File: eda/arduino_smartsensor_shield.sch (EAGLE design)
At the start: 10 parts, among them J1 ARDUINO_R3_SHIELD, J2 ISP

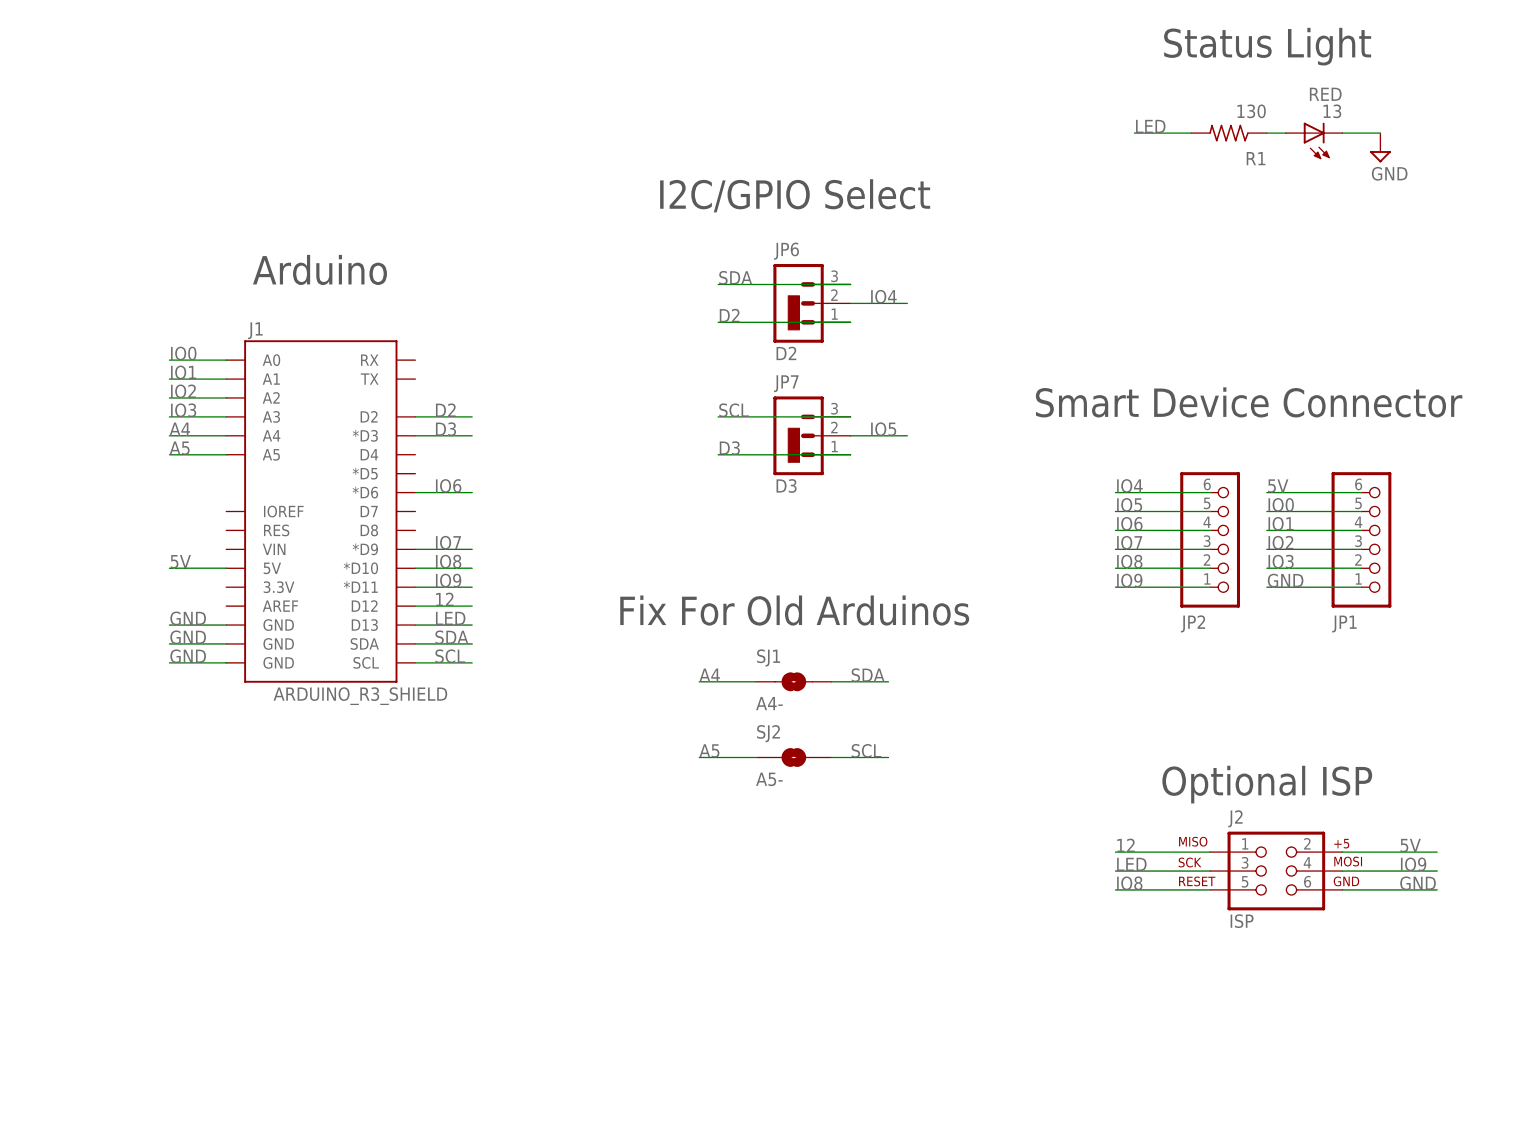
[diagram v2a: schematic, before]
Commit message: Revision B of Arduino smart device shield
- Add a connector for an external AVR programmer
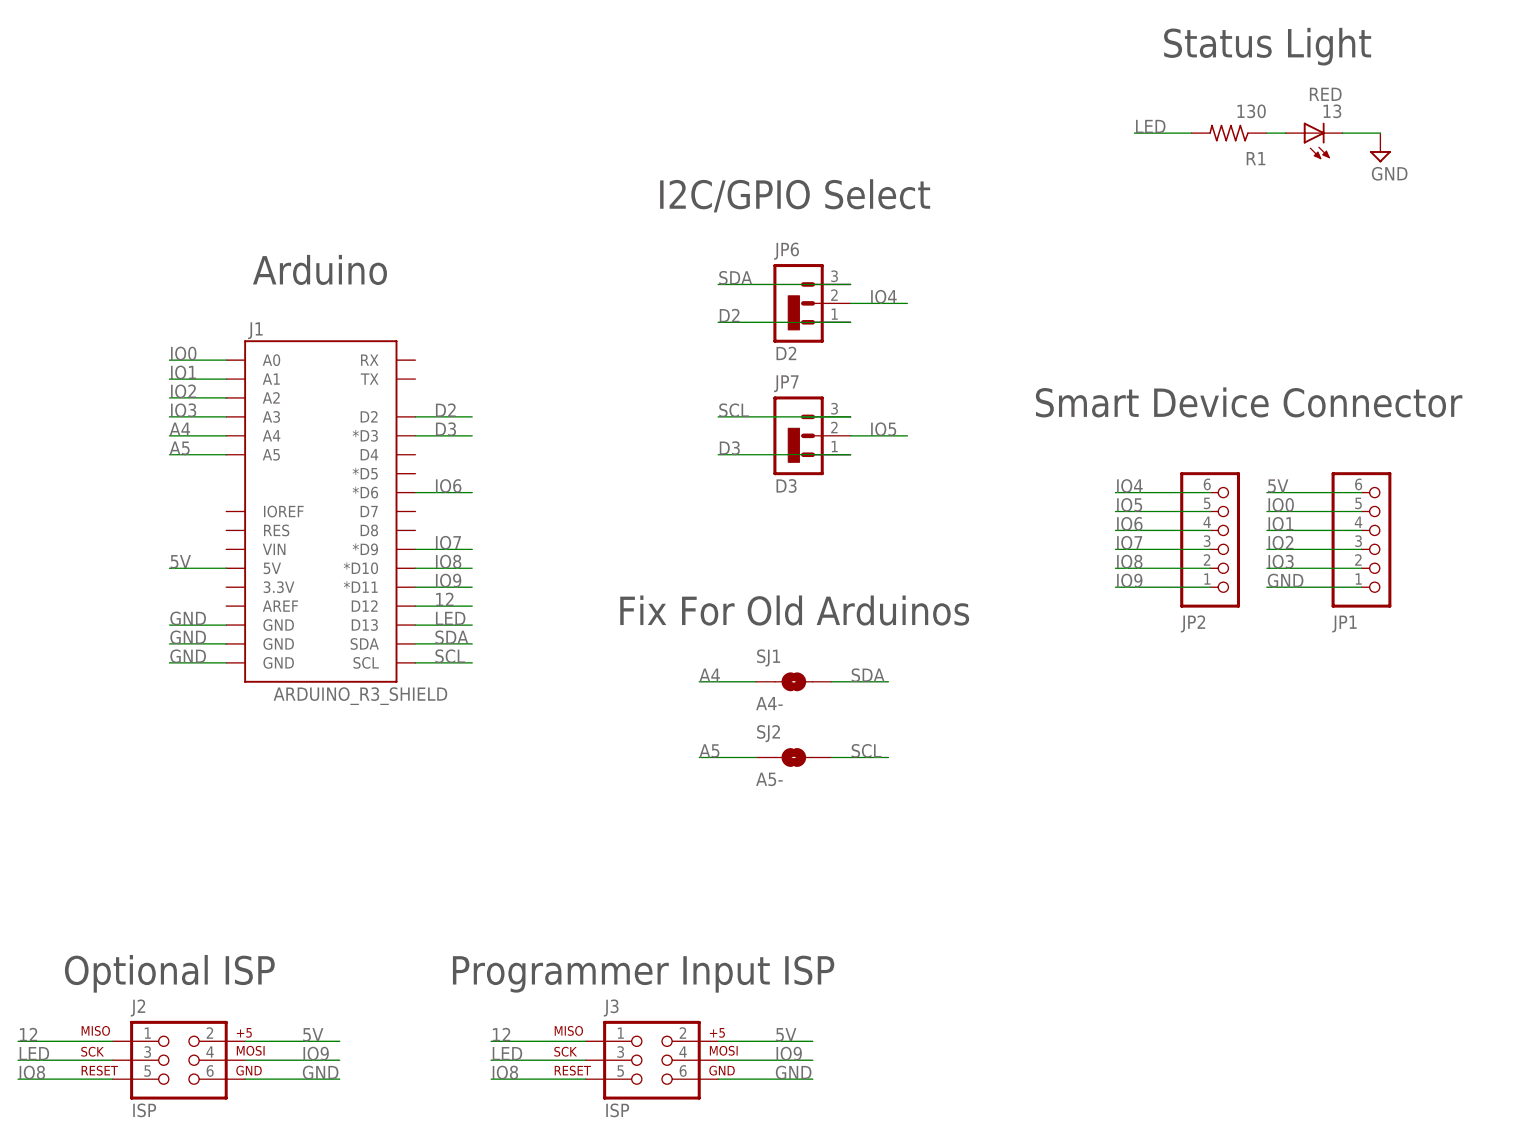
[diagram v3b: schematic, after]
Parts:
- added J3: ISP, pie:AVR_SPI_PRG_6PTH
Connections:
- net 12: now also J3.1
- net 5V: now also J3.2
- net GND: now also J3.6
- net IO8: now also J3.5
- net IO9: now also J3.4
- net LED: now also J3.3
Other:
- note added: "Programmer Input ISP"
- moved on the sheet: J2
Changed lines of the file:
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@@
 <part name="FRAME1" library="pie" deviceset="FRAME-LETTER" device="">
 <attribute name="AUTHOR" value="Casey Duckering"/>
-<attribute name="REVISION" value="1A"/>
+<attribute name="REVISION" value="1B"/>
 </part>
 <part name="R1" library="pie" deviceset="R-US_" device="R0603" value="130"/>
@@
 <part name="JP2" library="pie" deviceset="PINHD-1X6" device=""/>
 <part name="J2" library="pie" deviceset="AVR_SPI_PRG_6" device="PTH" value="ISP"/>
+<part name="J3" library="pie" deviceset="AVR_SPI_PRG_6" device="PTH" value="ISP"/>
 </parts>
 <sheets>
@@
 <text x="180.34" y="109.22" size="3.81" layer="97" font="vector" ratio="15" align="bottom-center">Smart Device Connector</text>
 <text x="182.88" y="157.48" size="3.81" layer="97" font="vector" ratio="15" align="bottom-center">Status Light</text>
-<text x="182.88" y="58.42" size="3.81" layer="97" font="vector" ratio="15" align="bottom-center">Optional ISP</text>
+<text x="35.56" y="33.02" size="3.81" layer="97" font="vector" ratio="15" align="bottom-center">Optional ISP</text>
+<text x="99.06" y="33.02" size="3.81" layer="97" font="vector" ratio="15" align="bottom-center">Programmer Input ISP</text>
 </plain>
 <instances>
@@
 <instance part="JP1" gate="A" x="195.58" y="92.71" rot="MR180"/>
 <instance part="JP2" gate="A" x="175.26" y="92.71" rot="MR180"/>
-<instance part="J2" gate="G$1" x="182.88" y="48.26"/>
+<instance part="J2" gate="G$1" x="35.56" y="22.86"/>
+<instance part="J3" gate="G$1" x="99.06" y="22.86"/>
 </instances>
 <busses>
@@
 <segment>
 <pinref part="J2" gate="G$1" pin="6"/>
-<wire x1="205.74" y1="45.72" x2="193.04" y2="45.72" width="0.1524" layer="91"/>
-<label x="200.66" y="45.72" size="1.778" layer="95"/>
+<wire x1="58.42" y1="20.32" x2="45.72" y2="20.32" width="0.1524" layer="91"/>
+<label x="53.34" y="20.32" size="1.778" layer="95"/>
+</segment>
+<segment>
+<pinref part="J3" gate="G$1" pin="6"/>
+<wire x1="121.92" y1="20.32" x2="109.22" y2="20.32" width="0.1524" layer="91"/>
+<label x="116.84" y="20.32" size="1.778" layer="95"/>
 </segment>
 </net>
@@
 <segment>
 <pinref part="J2" gate="G$1" pin="2"/>
-<wire x1="205.74" y1="50.8" x2="193.04" y2="50.8" width="0.1524" layer="91"/>
-<label x="200.66" y="50.8" size="1.778" layer="95"/>
+<wire x1="58.42" y1="25.4" x2="45.72" y2="25.4" width="0.1524" layer="91"/>
+<label x="53.34" y="25.4" size="1.778" layer="95"/>
+</segment>
+<segment>
+<pinref part="J3" gate="G$1" pin="2"/>
+<wire x1="121.92" y1="25.4" x2="109.22" y2="25.4" width="0.1524" layer="91"/>
+<label x="116.84" y="25.4" size="1.778" layer="95"/>
 </segment>
 </net>
@@
 <segment>
 <pinref part="J2" gate="G$1" pin="4"/>
-<wire x1="205.74" y1="48.26" x2="193.04" y2="48.26" width="0.1524" layer="91"/>
-<label x="200.66" y="48.26" size="1.778" layer="95"/>
+<wire x1="58.42" y1="22.86" x2="45.72" y2="22.86" width="0.1524" layer="91"/>
+<label x="53.34" y="22.86" size="1.778" layer="95"/>
+</segment>
+<segment>
+<pinref part="J3" gate="G$1" pin="4"/>
+<wire x1="121.92" y1="22.86" x2="109.22" y2="22.86" width="0.1524" layer="91"/>
+<label x="116.84" y="22.86" size="1.778" layer="95"/>
 </segment>
 </net>
@@
 <segment>
 <pinref part="J2" gate="G$1" pin="5"/>
-<wire x1="162.56" y1="45.72" x2="175.26" y2="45.72" width="0.1524" layer="91"/>
-<label x="162.56" y="45.72" size="1.778" layer="95"/>
+<wire x1="15.24" y1="20.32" x2="27.94" y2="20.32" width="0.1524" layer="91"/>
+<label x="15.24" y="20.32" size="1.778" layer="95"/>
+</segment>
+<segment>
+<pinref part="J3" gate="G$1" pin="5"/>
+<wire x1="78.74" y1="20.32" x2="91.44" y2="20.32" width="0.1524" layer="91"/>
+<label x="78.74" y="20.32" size="1.778" layer="95"/>
 </segment>
 </net>
@@
 <segment>
 <pinref part="J2" gate="G$1" pin="3"/>
-<wire x1="162.56" y1="48.26" x2="175.26" y2="48.26" width="0.1524" layer="91"/>
-<label x="162.56" y="48.26" size="1.778" layer="95"/>
+<wire x1="15.24" y1="22.86" x2="27.94" y2="22.86" width="0.1524" layer="91"/>
+<label x="15.24" y="22.86" size="1.778" layer="95"/>
+</segment>
+<segment>
+<pinref part="J3" gate="G$1" pin="3"/>
+<wire x1="78.74" y1="22.86" x2="91.44" y2="22.86" width="0.1524" layer="91"/>
+<label x="78.74" y="22.86" size="1.778" layer="95"/>
 </segment>
 </net>
@@
 <segment>
 <pinref part="J2" gate="G$1" pin="1"/>
-<wire x1="175.26" y1="50.8" x2="162.56" y2="50.8" width="0.1524" layer="91"/>
-<label x="162.56" y="50.8" size="1.778" layer="95"/>
+<wire x1="27.94" y1="25.4" x2="15.24" y2="25.4" width="0.1524" layer="91"/>
+<label x="15.24" y="25.4" size="1.778" layer="95"/>
 </segment>
 <segment>
@@
 <label x="71.12" y="83.82" size="1.778" layer="95"/>
 </segment>
-</net>
+<segment>
+<pinref part="J3" gate="G$1" pin="1"/>
+<wire x1="91.44" y1="25.4" x2="78.74" y2="25.4" width="0.1524" layer="91"/>
+<label x="78.74" y="25.4" size="1.778" layer="95"/>
+</segment>
+</net>
